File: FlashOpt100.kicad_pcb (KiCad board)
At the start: 2 copper layers, 16 x 38 mm, 9 parts, among them J1 Tandy_100_102_200_option_rom, U1 29F010

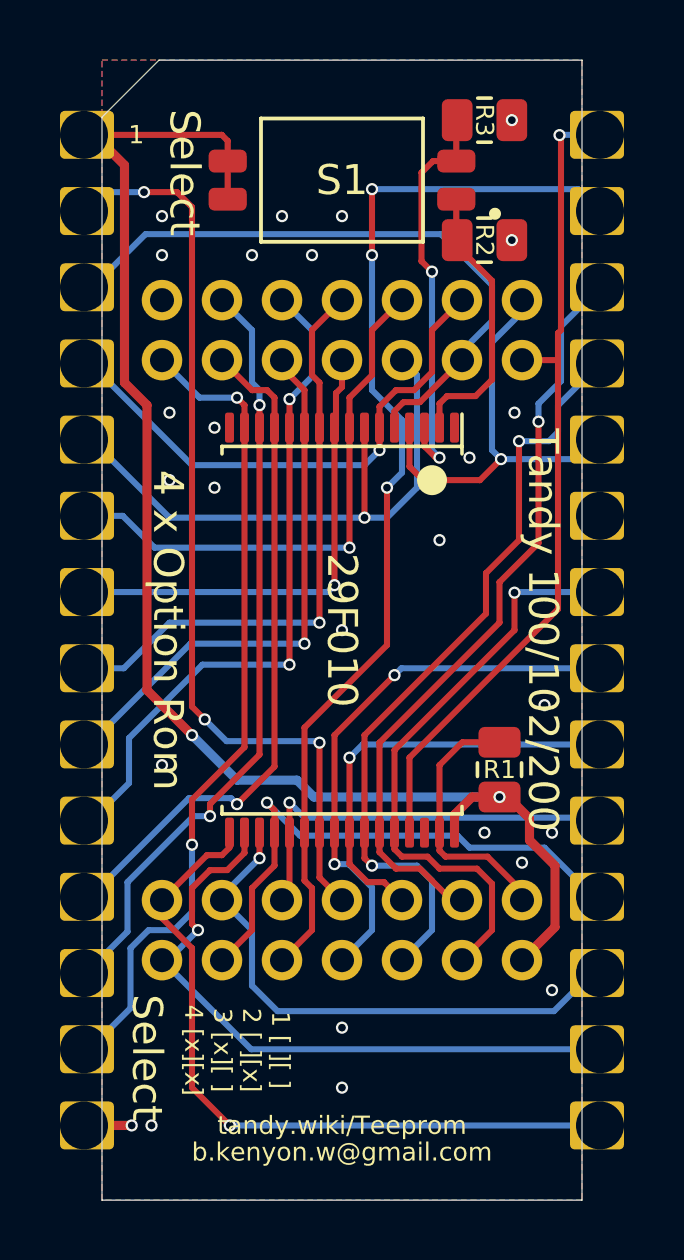
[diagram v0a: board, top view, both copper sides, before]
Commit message: FlashRom100 programming socket
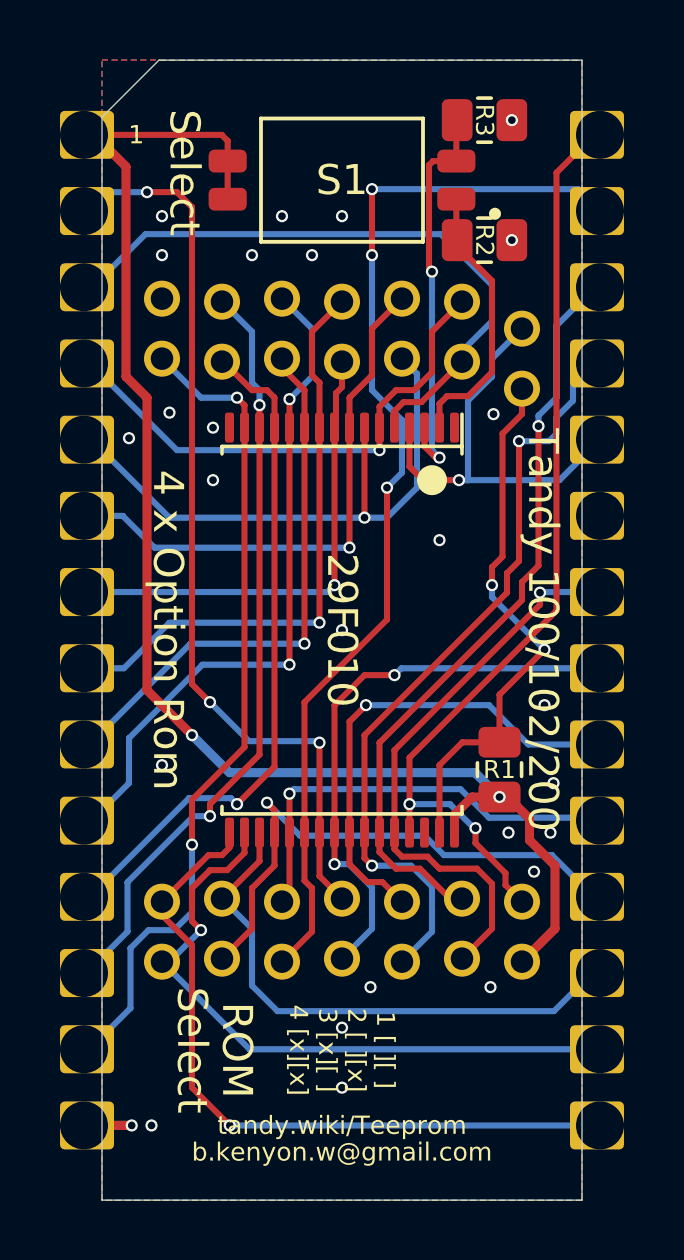
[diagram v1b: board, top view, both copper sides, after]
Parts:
- removed the REF** at (147.2, 109.2)
- removed the REF** at (147.2, 89.2)
- added REF**: 4x7_prg_2.0mm_female_staggered, 000_LOCAL:4x7_prg_2.0mm_female_staggered, F.Cu at (147.2, 99.2)
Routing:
- net /~WE: track 8.78 -> 18.1 mm, vias 0 -> 2
- net /A14: track 27.9 -> 32.0 mm, vias 1 -> 2
- net /A11: track 14.3 -> 16.1 mm
- net /D7: track 14.0 -> 14.6 mm
- net /A13: track 19.8 -> 19.2 mm
- net /~OE: track 18.5 -> 19.0 mm
- net /D5: vias 1 -> 0
- net GND: vias 26 -> 27
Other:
- board text added: "R1,R2,R3: 47k"
- board text added: "ROM"
- board text removed: "R1: 47k"
- board text removed: "Use with thingiverse.com/thing:3821586"

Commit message: FlashOpt100 programming port
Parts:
- J2: renamed from REF**; value 4x7_prg_2.0mm_female_staggered -> 29C256
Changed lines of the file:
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@@
     (add_net /~WE)
     (add_net GND)
+    (add_net "Net-(J1-Pad23)")
+    (add_net "Net-(J2-Pad14)")
+    (add_net "Net-(J2-Pad28)")
+    (add_net "Net-(U1-Pad1)")
+    (add_net "Net-(U1-Pad30)")
     (add_net VCC)
+  )
+  (module 000_LOCAL:SW_DS05-127-2-02BK-SMT-TR (layer Top)
+    (at 147.2184 84.187 180)
+    (fp_text reference S1 (at 0 0) (layer F.SilkS)
+      (effects (font (size 1 1) (thickness 0.1)))
+    )
+    (fp_text value 2xSPST (at 12.175 3.065) (layer F.Fab)
+      (effects (font (size 1 1) (thickness 0.015)))
+    )
+    (fp_circle (center -2.1 -0.65) (end -2 -0.65) (layer F.Fab) (width 0.2))
+    (fp_circle (center -2.1 -0.65) (end -2 -0.65) (layer F.SilkS) (width 0.2))
+    (fp_line (start 4.695 -2.305) (end -4.695 -2.305) (layer F.CrtYd) (width 0.05))
+    (fp_line (start 4.695 2.305) (end 4.695 -2.305) (layer F.CrtYd) (width 0.05))
+    (fp_line (start -4.695 2.305) (end 4.695 2.305) (layer F.CrtYd) (width 0.05))
+    (fp_line (start -4.695 -2.305) (end -4.695 2.305) (layer F.CrtYd) (width 0.05))
+    (fp_line (start -2.7 2.055) (end -2.7 -2.055) (layer F.SilkS) (width 0.127))
+    (fp_line (start 2.7 2.055) (end -2.7 2.055) (layer F.SilkS) (width 0.127))
+    (fp_line (start 2.7 -2.055) (end 2.7 2.055) (layer F.SilkS) (width 0.127))
+    (fp_line (start -2.7 -2.055) (end 2.7 -2.055) (layer F.SilkS) (width 0.127))
+    (fp_line (start -2.7 2.055) (end -2.7 -2.055) (layer F.Fab) (width 0.127))
+    (fp_line (start 2.7 2.055) (end -2.7 2.055) (layer F.Fab) (width 0.127))
+    (fp_line (start 2.7 -2.055) (end 2.7 2.055) (layer F.Fab) (width 0.127))
+    (fp_line (start -2.7 -2.055) (end 2.7 -2.055) (layer F.Fab) (width 0.127))
+    (pad 1B smd roundrect (at 3.81 -0.635 180) (size 1.27 0.76) (layers Top F.Paste F.Mask) (roundrect_rratio 0.25)
+      (net 27 VCC))
+    (pad 2B smd roundrect (at 3.81 0.635 180) (size 1.27 0.76) (layers Top F.Paste F.Mask) (roundrect_rratio 0.25)
+      (net 27 VCC))
+    (pad 2A smd roundrect (at -3.81 0.635 180) (size 1.27 0.76) (layers Top F.Paste F.Mask) (roundrect_rratio 0.25)
+      (net 29 /A15))
+    (pad 1A smd roundrect (at -3.81 -0.635 180) (size 1.27 0.76) (layers Top F.Paste F.Mask) (roundrect_rratio 0.25)
+      (net 30 /A16))
+    (model ${KIPRJMOD}/000_LOCAL.pretty/3d/CUI_DEVICES_DS05-127-2-02BK-SMT-TR.step
+      (offset (xyz -9.65 -1.1 -1.5))
+      (scale (xyz 1 1 1))
+      (rotate (xyz -90 0 0))
+    )
   )
   (module 000_LOCAL:pcb2molex8878 (layer Top)
@@
     (descr "Through hole straight pin header, 2x07, 2.00mm pitch, double rows")
     (tags "Through hole pin header THT 2x07 2.00mm double row")
-    (fp_text reference REF** (at 0 6 270 unlocked) (layer F.SilkS) hide
+    (fp_text reference J2 (at 0 6 270 unlocked) (layer F.SilkS) hide
       (effects (font (size 1 1) (thickness 0.15)))
     )
-    (fp_text value 4x7_prg_2.0mm_female_staggered (at 0 8 90) (layer F.Fab)
+    (fp_text value 29C256 (at 0 8 90) (layer F.Fab)
       (effects (font (size 1 1) (thickness 0.15)))
     )
@@
     )
   )
-  (module 000_LOCAL:SW_DS05-127-2-02BK-SMT-TR (layer Top)
-    (at 147.2184 84.187 180)
-    (fp_text reference S1 (at 0 0) (layer F.SilkS)
-      (effects (font (size 1 1) (thickness 0.1)))
-    )
-    (fp_text value 2xSPST (at 12.175 3.065) (layer F.Fab)
-      (effects (font (size 1 1) (thickness 0.015)))
-    )
-    (fp_line (start -2.7 -2.055) (end 2.7 -2.055) (layer F.Fab) (width 0.127))
-    (fp_line (start 2.7 -2.055) (end 2.7 2.055) (layer F.Fab) (width 0.127))
-    (fp_line (start 2.7 2.055) (end -2.7 2.055) (layer F.Fab) (width 0.127))
-    (fp_line (start -2.7 2.055) (end -2.7 -2.055) (layer F.Fab) (width 0.127))
-    (fp_line (start -2.7 -2.055) (end 2.7 -2.055) (layer F.SilkS) (width 0.127))
-    (fp_line (start 2.7 -2.055) (end 2.7 2.055) (layer F.SilkS) (width 0.127))
-    (fp_line (start 2.7 2.055) (end -2.7 2.055) (layer F.SilkS) (width 0.127))
-    (fp_line (start -2.7 2.055) (end -2.7 -2.055) (layer F.SilkS) (width 0.127))
-    (fp_line (start -4.695 -2.305) (end -4.695 2.305) (layer F.CrtYd) (width 0.05))
-    (fp_line (start -4.695 2.305) (end 4.695 2.305) (layer F.CrtYd) (width 0.05))
-    (fp_line (start 4.695 2.305) (end 4.695 -2.305) (layer F.CrtYd) (width 0.05))
-    (fp_line (start 4.695 -2.305) (end -4.695 -2.305) (layer F.CrtYd) (width 0.05))
-    (fp_circle (center -5.1 -1.12) (end -5 -1.12) (layer F.SilkS) (width 0.2))
-    (fp_circle (center -5.1 -1.12) (end -5 -1.12) (layer F.Fab) (width 0.2))
-    (pad 1B smd roundrect (at 3.81 -0.635 180) (size 1.27 0.76) (layers Top F.Paste F.Mask) (roundrect_rratio 0.25)
-      (net 27 VCC))
-    (pad 2B smd roundrect (at 3.81 0.635 180) (size 1.27 0.76) (layers Top F.Paste F.Mask) (roundrect_rratio 0.25)
-      (net 27 VCC))
-    (pad 2A smd roundrect (at -3.81 0.635 180) (size 1.27 0.76) (layers Top F.Paste F.Mask) (roundrect_rratio 0.25)
-      (net 29 /A15))
-    (pad 1A smd roundrect (at -3.81 -0.635 180) (size 1.27 0.76) (layers Top F.Paste F.Mask) (roundrect_rratio 0.25)
-      (net 30 /A16))
-    (model ${KIPRJMOD}/000_LOCAL.pretty/3d/CUI_DEVICES_DS05-127-2-02BK-SMT-TR.step
-      (offset (xyz -9.65 -1.1 -1.5))
-      (scale (xyz 1 1 1))
-      (rotate (xyz -90 0 0))
-    )
-  )

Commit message: programming adapter
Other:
- board text added: "FlashOpt100"
